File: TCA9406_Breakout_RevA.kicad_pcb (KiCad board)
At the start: 2 copper layers, 30 x 19 mm, 32 parts, among them J1 Connector A, J2 Connector B, U1 TCA9406DC

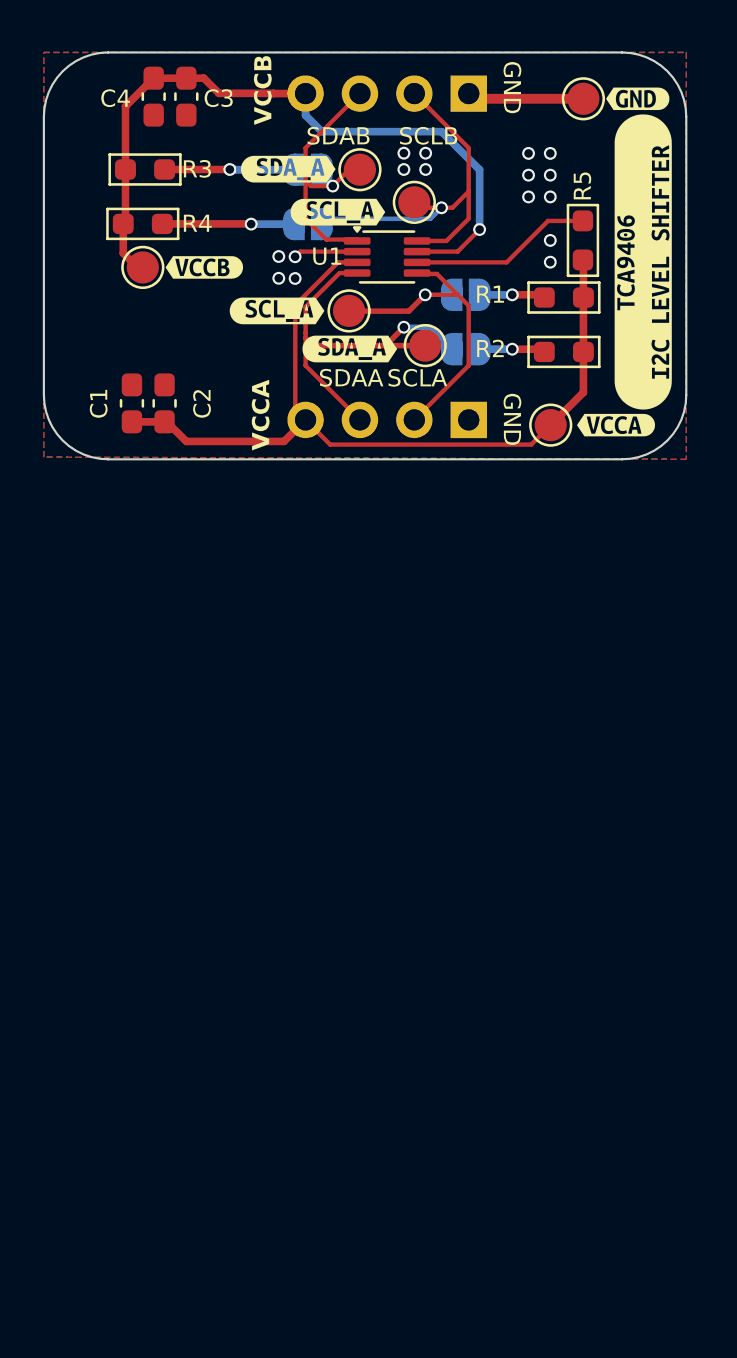
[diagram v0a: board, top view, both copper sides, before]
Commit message: minor layout change
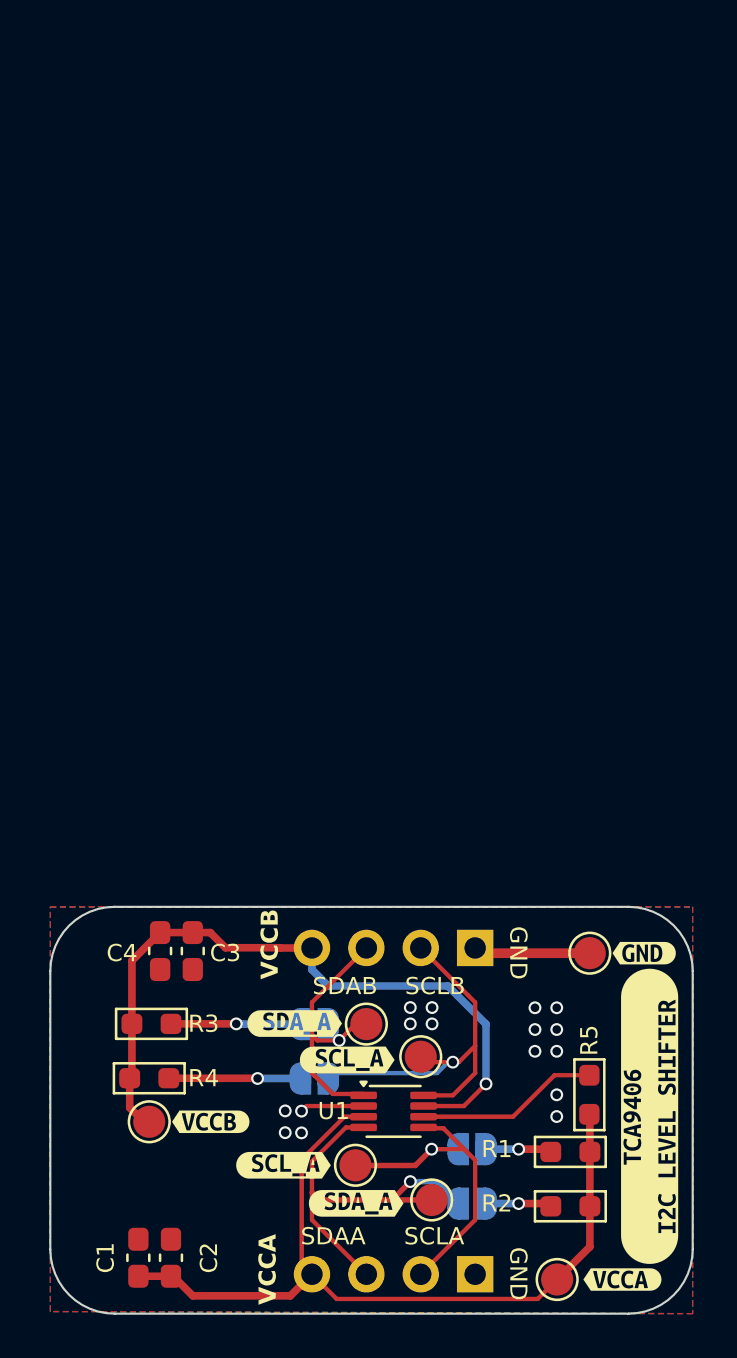
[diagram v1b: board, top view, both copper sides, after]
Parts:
- moved J1 39.9 mm to (150.1, 97.1)
- moved JP2 39.9 mm to (150.0, 91.2)
- moved JP3 39.9 mm to (142.6, 85.4)
- moved R1 39.9 mm to (154.6, 93.9)
- moved R4 39.9 mm to (134.9, 87.9)
- moved TP3 39.9 mm to (134.9, 89.9)
- moved TP4 39.9 mm to (148.1, 93.6)
- moved TP5 39.9 mm to (145.1, 85.4)
- moved TP7 39.9 mm to (147.6, 86.9)
- moved kibuzzard-6A3518B1 39.9 mm to (144.6, 93.7)
- moved kibuzzard-6A3518B1 39.9 mm to (141.7, 85.4)
- moved kibuzzard-6A3518C1 39.9 mm to (137.8, 89.9)
- moved C1 39.9 mm to (134.4, 96.3)
- moved C2 39.9 mm to (135.9, 96.3)
- moved C3 39.9 mm to (137.0, 82.0)
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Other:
- board text added: "SCL_A"
- board text added: "SDA_A"

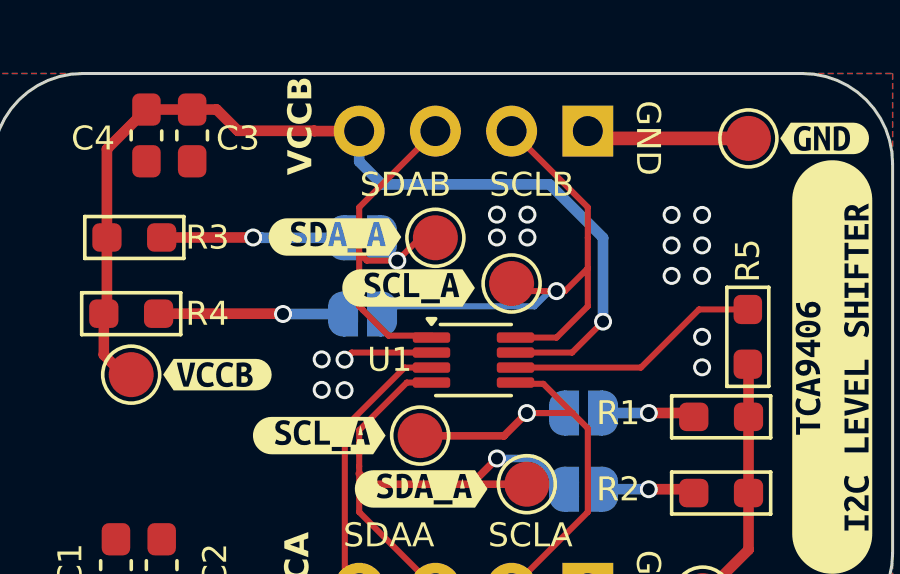
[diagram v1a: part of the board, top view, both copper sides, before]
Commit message: Fixing ground plane
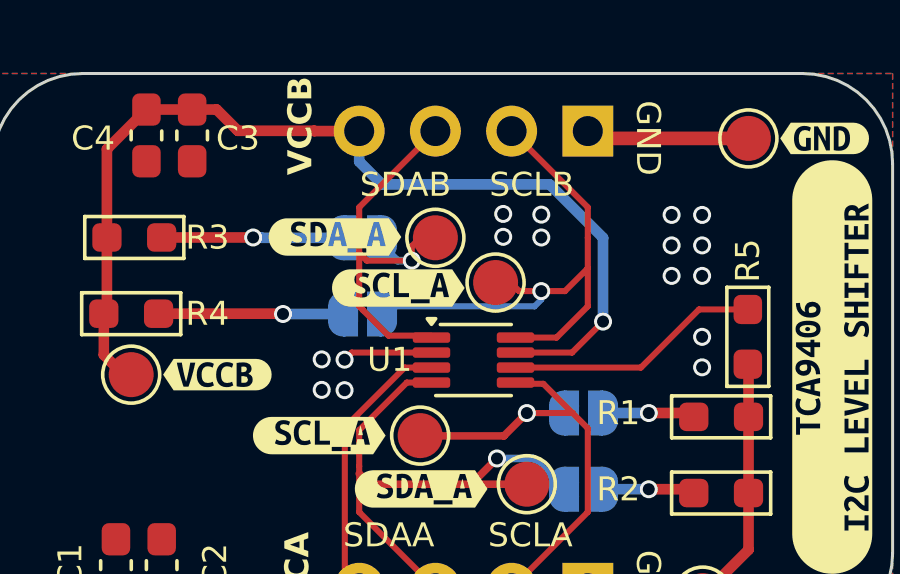
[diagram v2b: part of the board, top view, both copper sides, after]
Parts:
- moved TP7 0.53 mm to (147.1, 86.9)
- moved kibuzzard-6A3518B8 0.34 mm to (143.8, 87.0)
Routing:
- net /SDA_B: track 13.7 -> 14.5 mm
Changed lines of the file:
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@@
 	(footprint "TestPoint:TestPoint_Pad_D1.5mm"
 		(layer "F.Cu")
-		(at 147.6 86.9)
+		(at 147.066 86.868)
 		(descr "SMD pad as test Point, diameter 1.5mm")
 		(tags "test point SMD pad")
@@
 	(footprint "kibuzzard-6A3518B8"
 		(layer "F.Cu")
-		(at 144.166654 87.049895)
+		(at 143.824762 87.049895)
 		(descr "Generated with KiBuzzard")
 		(tags "kb_params=eyJBbGlnbm1lbnRDaG9pY2UiOiAiQ2VudGVyIiwgIkNhcExlZnRDaG9pY2UiOiAiKCIsICJDYXBSaWdodENob2ljZSI6ICI+IiwgIkZvbnRDb21ib0JveCI6ICJVYnVudHVNb25vLUIiLCAiSGVpZ2h0Q3RybCI6IDAuOCwgIkxheWVyQ29tYm9Cb3giOiAiRi5TaWxrUyIsICJMaW5lU3BhY2luZ0N0cmwiOiAxLjUsICJNdWx0aUxpbmVUZXh0IjogIlNDTF9BIiwgIlBhZGRpbmdCb3R0b21DdHJsIjogMS4wLCAiUGFkZGluZ0xlZnRDdHJsIjogMS4wLCAiUGFkZGluZ1JpZ2h0Q3RybCI6IDEuMCwgIlBhZGRpbmdUb3BDdHJsIjogMS4wLCAiV2lkdGhDdHJsIjogMC44LCAiYWR2YW5jZWRDaGVja2JveCI6IGZhbHNlLCAiaW5saW5lRm9ybWF0VGV4dGJveCI6IGZhbHNlLCAibGluZW92ZXJTdHlsZUNob2ljZSI6ICJSb3VuZGVkIiwgImxpbmVvdmVyVGhpY2tuZXNzQ3RybCI6IDF9")
@@
 			(keep_text_aligned yes)
 		)
-		(gr_text "7.62"
+		(gr_text "300"
 			(at 219.63 90.19 90)
 			(layer "Dwgs.User")
@@
 			(keep_text_aligned yes)
 		)
-		(gr_text "30"
+		(gr_text "1181.1024"
 			(at 145.3 73.45 0)
 			(layer "User.1")
@@
 			(keep_text_aligned yes)
 		)
-		(gr_text "19"
+		(gr_text "748.0315"
 			(at 171.45 89.4 90)
 			(layer "User.1")
@@
 	)
 	(via
-		(at 147.112 84.604)
+		(at 147.32 84.582)
 		(size 0.6)
 		(drill 0.4)
@@
 	)
 	(via
-		(at 148.128 84.604)
+		(at 148.59 84.604)
 		(size 0.6)
 		(drill 0.4)
@@
 	)
 	(via
-		(at 147.112 85.366)
+		(at 147.32 85.344)
 		(size 0.6)
 		(drill 0.4)
@@
 	)
 	(via
-		(at 148.128 85.366)
+		(at 148.59 85.366)
 		(size 0.6)
 		(drill 0.4)
@@
 	)
 	(segment
-		(start 149.098 87.154)
-		(end 147.854 87.154)
+		(start 149.378 87.154)
+		(end 150.14 86.392)
 		(width 0.2032)
 		(layer "F.Cu")
@@
 	)
 	(segment
-		(start 147.854 87.154)
-		(end 147.6 86.9)
+		(start 150.14 86.392)
+		(end 150.14 87.662)
 		(width 0.2032)
 		(layer "F.Cu")
@@
 	)
 	(segment
-		(start 150.14 86.392)
-		(end 150.14 87.662)
+		(start 148.59 87.154)
+		(end 149.378 87.154)
 		(width 0.2032)
 		(layer "F.Cu")
@@
 	)
 	(segment
-		(start 150.14 84.36)
-		(end 150.14 85.376)
+		(start 148.59 87.154)
+		(end 147.854 87.154)
 		(width 0.2032)
 		(layer "F.Cu")
@@
 	)
 	(segment
-		(start 149.378 87.154)
-		(end 150.14 86.392)
+		(start 150.14 84.36)
+		(end 150.14 85.376)
 		(width 0.2032)
 		(layer "F.Cu")
@@
 	)
 	(segment
-		(start 149.098 87.154)
-		(end 149.378 87.154)
+		(start 147.854 87.154)
+		(end 147.6 86.9)
 		(width 0.2032)
 		(layer "F.Cu")
@@
 	)
 	(via
-		(at 149.098 87.154)
+		(at 148.59 87.154)
 		(size 0.6)
 		(drill 0.4)
@@
 	)
 	(segment
-		(start 148.362 87.662)
-		(end 143.282 87.662)
+		(start 148.59 87.434)
+		(end 148.362 87.662)
 		(width 0.2032)
 		(layer "B.Cu")
@@
 	)
 	(segment
-		(start 148.87 87.154)
-		(end 148.362 87.662)
+		(start 148.59 87.154)
+		(end 148.59 87.434)
 		(width 0.2032)
 		(layer "B.Cu")
@@
 	)
 	(segment
-		(start 149.098 87.154)
-		(end 148.87 87.154)
+		(start 148.362 87.662)
+		(end 143.282 87.662)
 		(width 0.2032)
 		(layer "B.Cu")
@@
 	)
 	(segment
-		(start 142.52 85.884)
-		(end 142.52 87.662)
+		(start 144.272 86.138)
+		(end 144.272 85.656)
 		(width 0.2032)
 		(layer "F.Cu")
@@
 	)
 	(segment
-		(start 142.52 87.662)
-		(end 142.647 87.789)
+		(start 142.52 85.884)
+		(end 142.52 87.662)
 		(width 0.2032)
 		(layer "F.Cu")
@@
 	)
 	(segment
-		(start 142.774 86.138)
-		(end 142.52 85.884)
+		(start 142.52 87.662)
+		(end 142.647 87.789)
 		(width 0.2032)
 		(layer "F.Cu")
@@
 	)
 	(segment
-		(start 142.647 87.789)
-		(end 143.4952 88.6372)
+		(start 144.272 85.656)
+		(end 144.806 85.122)
 		(width 0.2032)
 		(layer "F.Cu")
@@
 	)
 	(segment
-		(start 142.52 84.36)
+		(start 142.774 86.138)
 		(end 142.52 85.884)
 		(width 0.2032)
@@
 	)
 	(segment
-		(start 143.79 86.138)
-		(end 144.806 85.122)
+		(start 142.647 87.789)
+		(end 143.4952 88.6372)
 		(width 0.2032)
 		(layer "F.Cu")
@@
 	)
 	(segment
-		(start 143.79 86.138)
+		(start 144.272 86.138)
 		(end 142.774 86.138)
 		(width 0.2032)
@@
 	)
 	(segment
+		(start 142.52 84.36)
+		(end 142.52 85.884)
+		(width 0.2032)
+		(layer "F.Cu")
+		(net 7)
+	)
+	(segment
 		(start 143.4952 88.6372)
 		(end 144.93 88.6372)
@@
 	)
 	(via
-		(at 143.79 86.138)
+		(at 144.272 86.138)
 		(size 0.6)
 		(drill 0.4)
@@
 	(segment
 		(start 143.282 85.63)
+		(end 143.282 85.122)
+		(width 0.254)
+		(layer "B.Cu")
+		(net 7)
+	)
+	(segment
+		(start 144.272 86.138)
 		(end 143.79 86.138)
 		(width 0.254)
@@
 	)
 	(segment
-		(start 143.282 85.122)
+		(start 143.79 86.138)
 		(end 143.282 85.63)
 		(width 0.254)

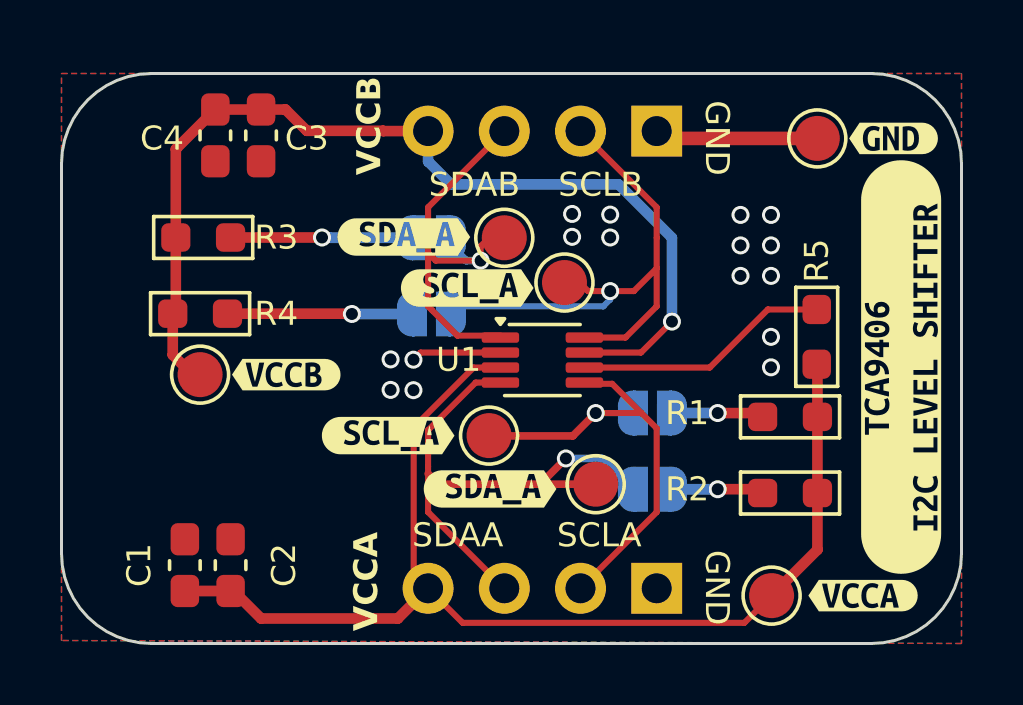
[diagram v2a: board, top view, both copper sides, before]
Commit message: Add comprehensive README.md
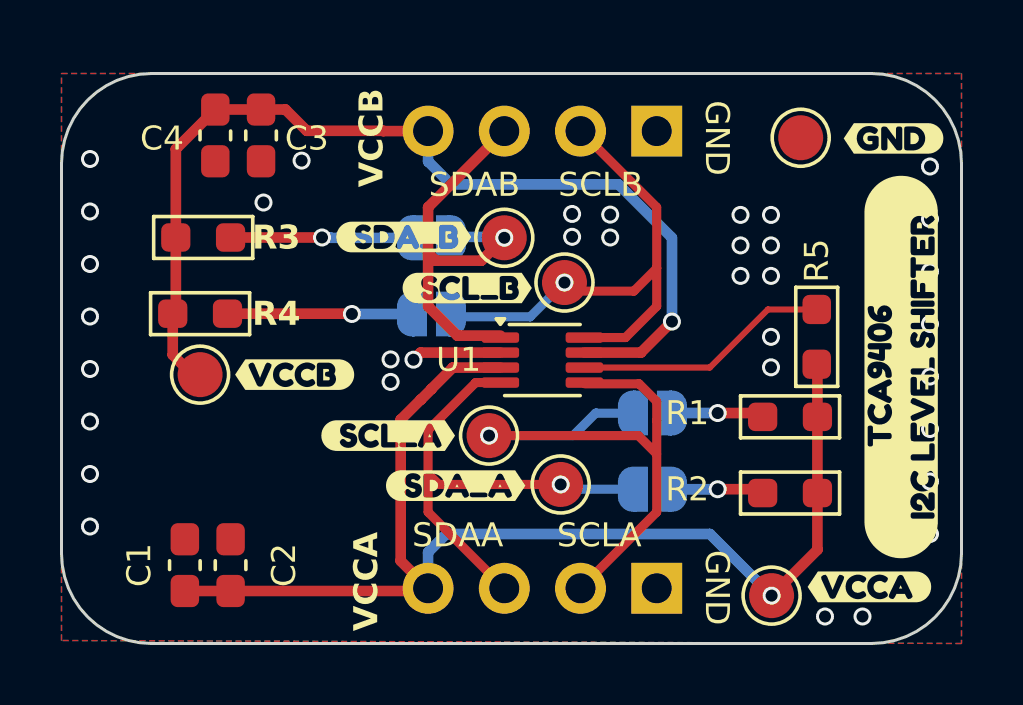
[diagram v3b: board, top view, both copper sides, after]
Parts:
- removed kibuzzard-6A3518B1 (x2): G***, kibuzzard-6A3518B1
- removed kibuzzard-6A3518B8 (x2): G***, kibuzzard-6A3518B8
- removed kibuzzard-6A3518C1: G***, kibuzzard-6A3518C1
- removed kibuzzard-6A3518D8: G***, kibuzzard-6A3518D8
- removed kibuzzard-6A351987: G***, kibuzzard-6A351987
- removed kibuzzard-6A351991: G***, kibuzzard-6A351991
- added kibuzzard-6A3A9CA2: G***, kibuzzard-6A3A9CA2, F.Cu at (143.8, 87.0)
- added kibuzzard-6A3A9CA9: G***, kibuzzard-6A3A9CA9, F.Cu at (141.7, 85.4)
- added kibuzzard-6A3A9CB1: G***, kibuzzard-6A3A9CB1, F.Cu at (143.4, 93.6)
- added kibuzzard-6A3A9CB7: G***, kibuzzard-6A3A9CB7, F.Cu at (141.2, 92.0)
- added kibuzzard-6A3A9CE7: G***, kibuzzard-6A3A9CE7, F.Cu at (138.1, 89.9)
- added kibuzzard-6A3A9CEE: G***, kibuzzard-6A3A9CEE, F.Cu at (157.2, 97.0)
- added kibuzzard-6A3A9D00: G***, kibuzzard-6A3A9D00, F.Cu at (158.3, 89.7)
- added kibuzzard-6A3A9D08: G***, kibuzzard-6A3A9D08, F.Cu at (158.0, 82.1)
- C1, C3: value 1u -> 1uF
- C2, C4: value 100n -> 100nF
- moved TP4 1.17 mm to (146.9, 93.6)
- moved TP1 0.55 mm to (154.9, 82.0)
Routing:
- net GND: track 8.45 -> 3.00 mm, vias 16 -> 35
- net /SCL_A: track 15.8 -> 21.1 mm
- net /SDA_A: track 19.0 -> 16.4 mm
- net VCCA: track 38.8 -> 40.3 mm, vias 0 -> 1
- net /SCL_B: track 18.4 -> 17.5 mm
